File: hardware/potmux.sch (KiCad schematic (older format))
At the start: 8 parts, among them P1 SOCKET_LEFT, P3 SOCKET_RIGHT, P4 KEYMAN64, U1 4052, U2 4052

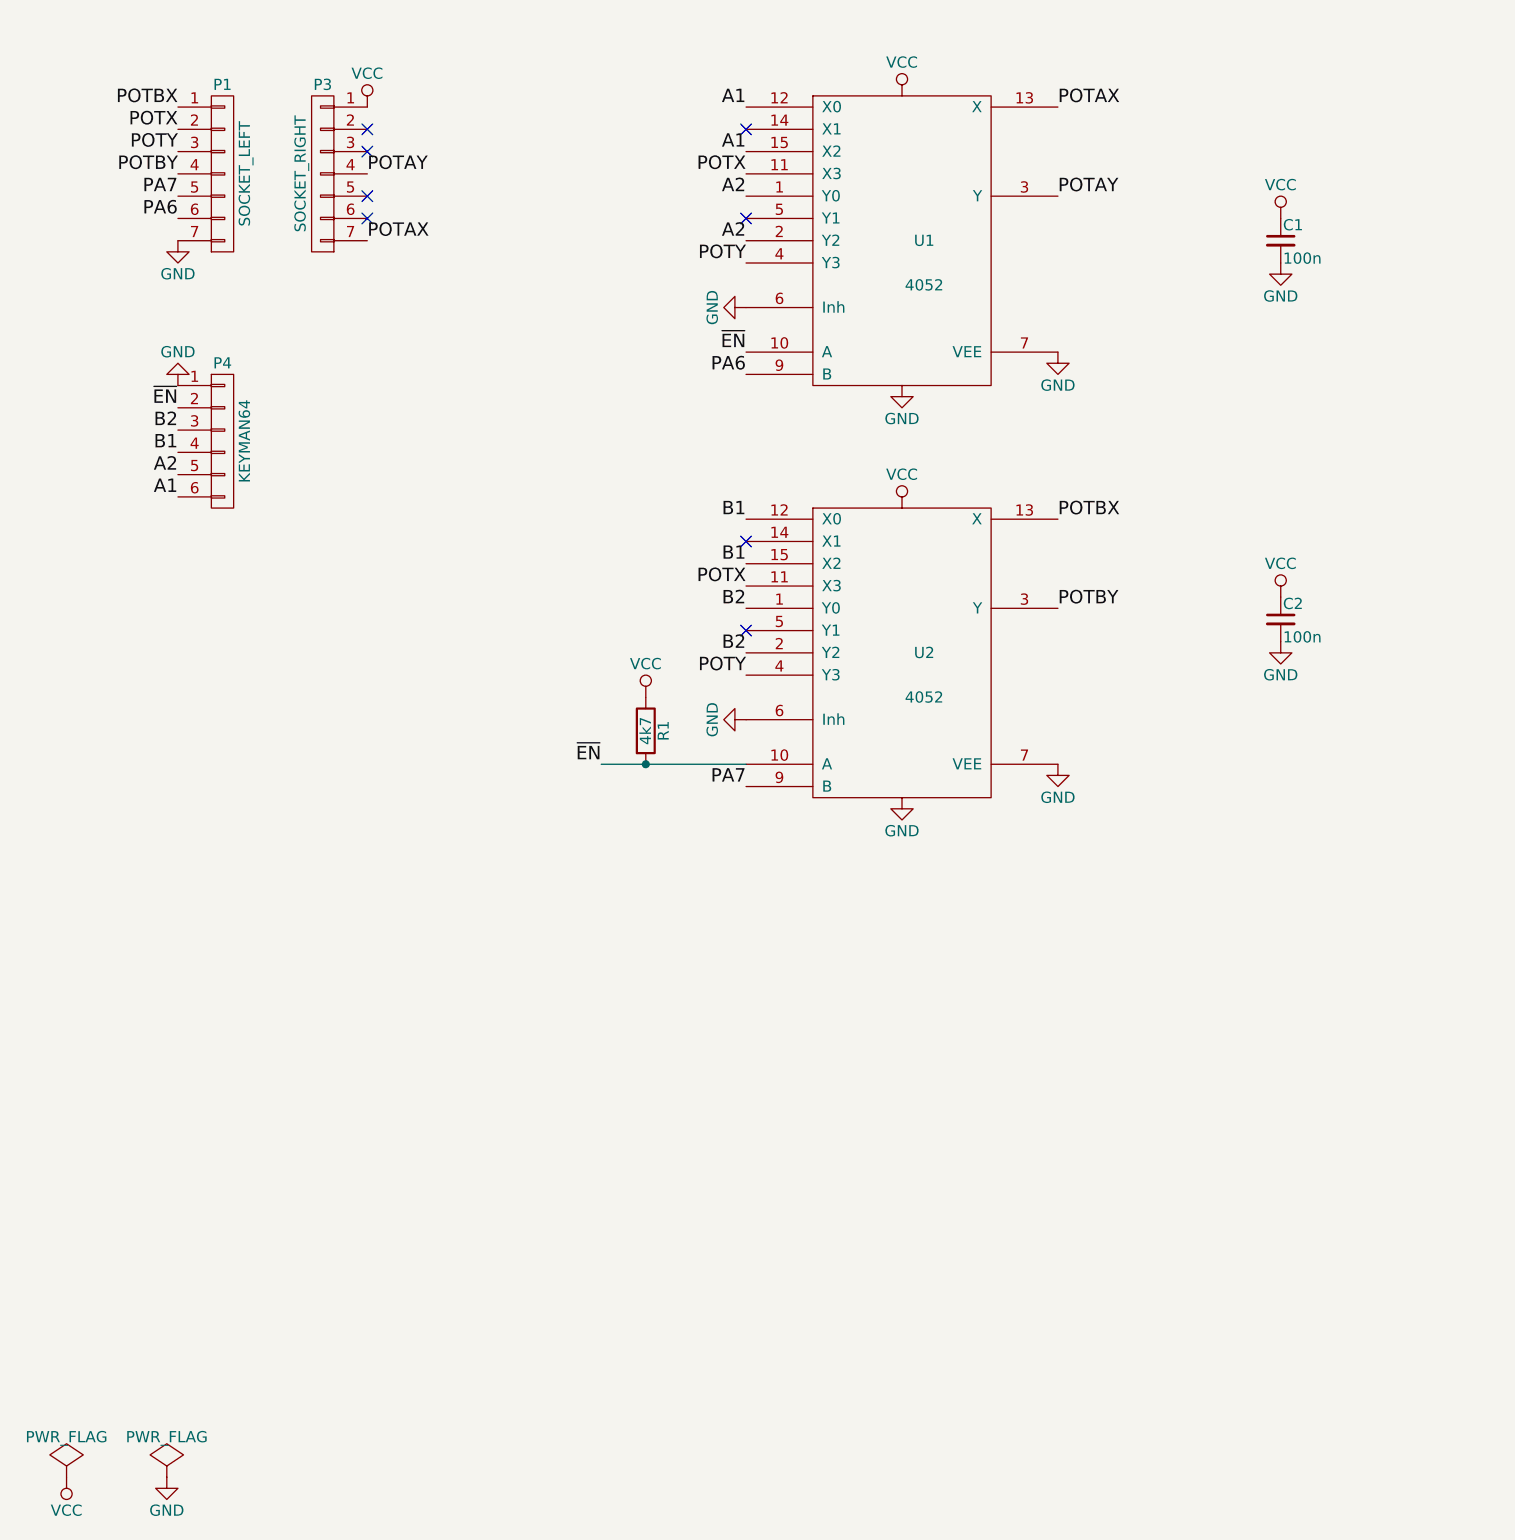
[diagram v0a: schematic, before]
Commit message: Improved layout, silk screen
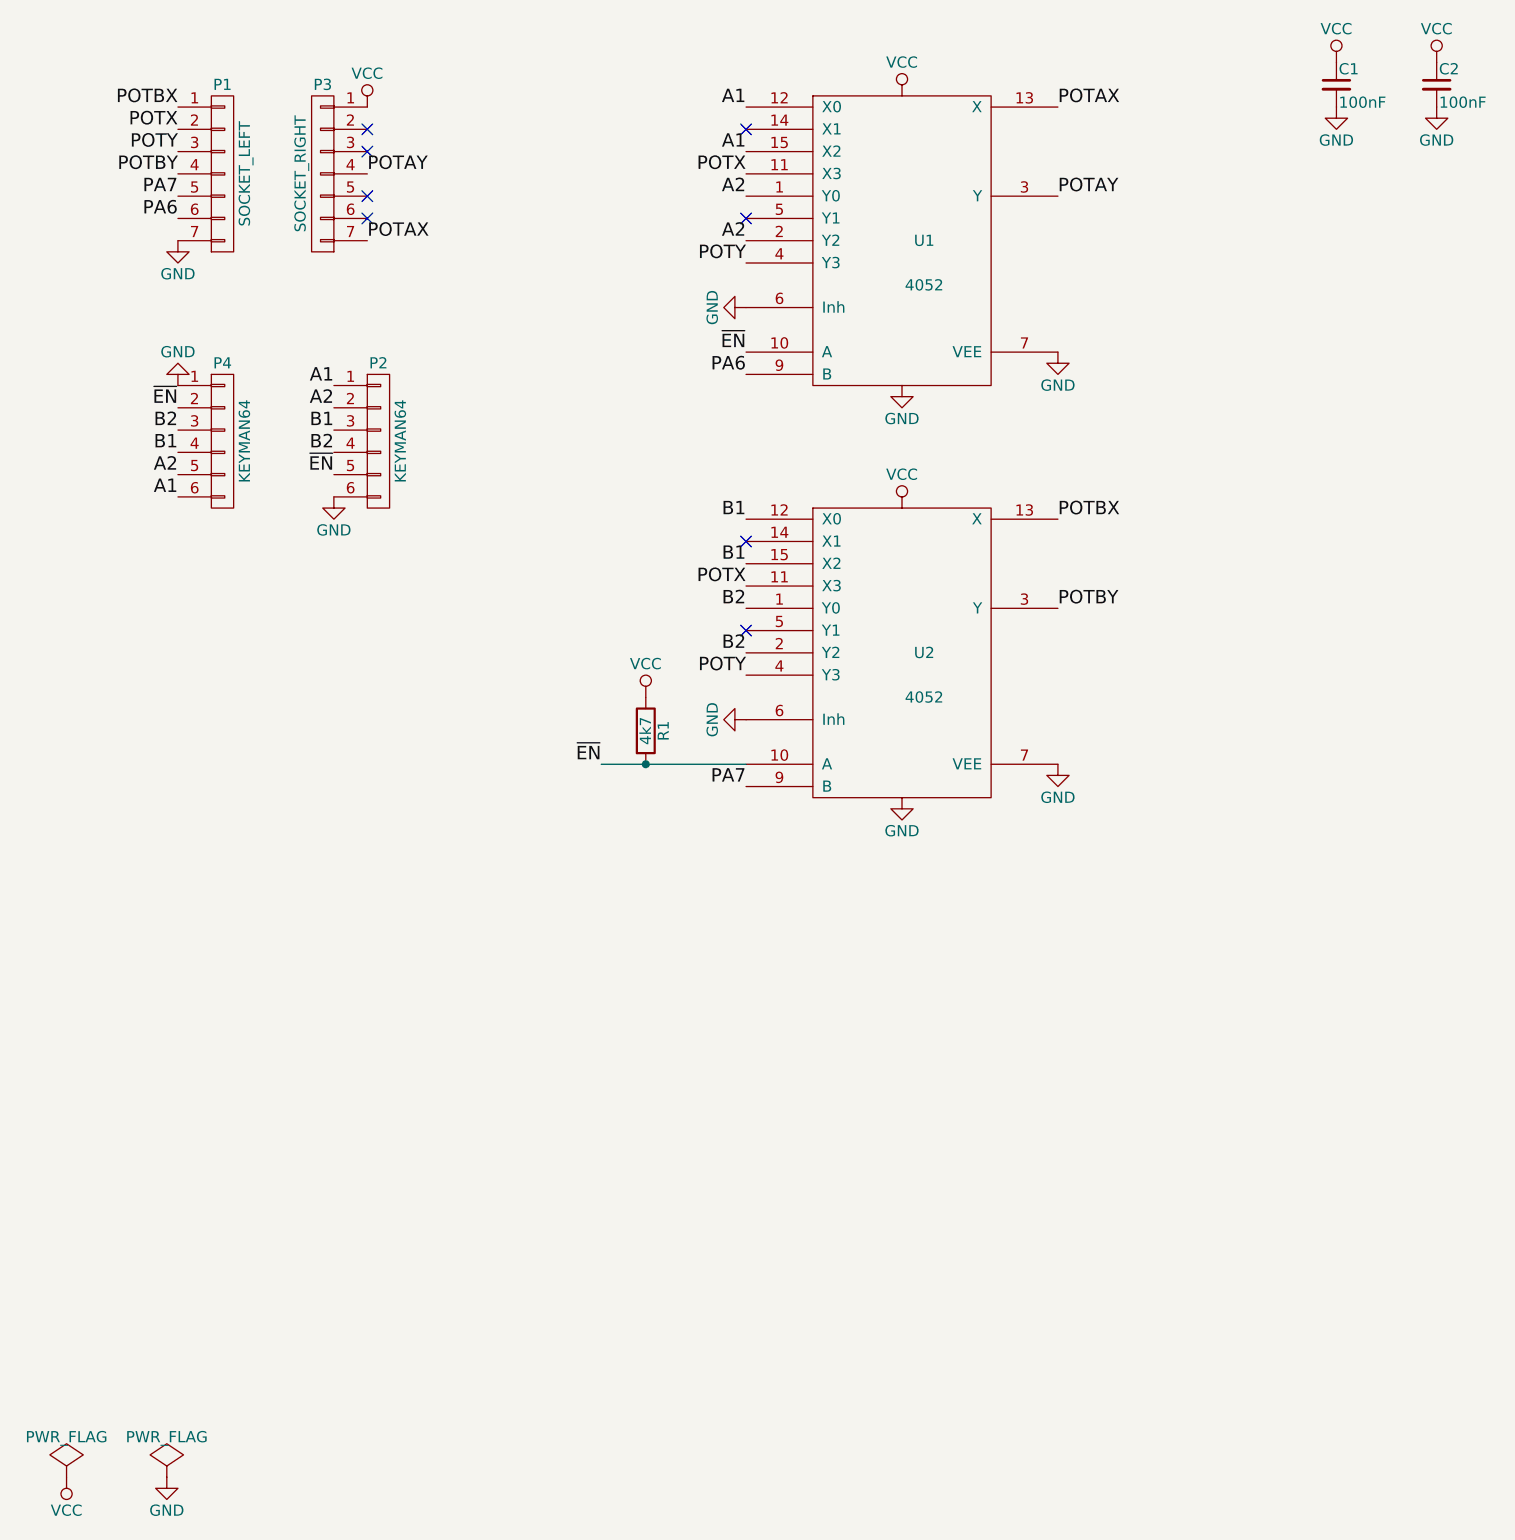
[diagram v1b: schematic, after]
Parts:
- added P2: KEYMAN64, Pin_Headers:Pin_Header_Angled_1x06_Pitch2.54mm, symbol CONN_01X06
- C1, C2: value 100n -> 100nF; footprint Capacitors_ThroughHole:C_Disc_D3.0mm_W1.6mm_P2.50mm -> Capacitors_SMD:C_0805_HandSoldering
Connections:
- net A1: now also P2.1 (P1)
- net A2: now also P2.2 (P2)
- net B1: now also P2.3 (P3)
- net B2: now also P2.4 (P4)
- net GND: now also P2.6 (P6)
- net ~EN: now also P2.5 (P5)
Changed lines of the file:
@@
 $Comp
 L VCC #PWR011
-U 1 1 580E8B82
-P 6200 1850
-F 0 "#PWR011" H 6200 1700 50  0001 C CNN
-F 1 "VCC" H 6200 2000 50  0000 C CNN
-F 2 "" H 6200 1850 50  0000 C CNN
-F 3 "" H 6200 1850 50  0000 C CNN
-	1    6200 1850
-	1    0    0    -1
-$EndComp
-$Comp
-L C_Small C1
-U 1 1 580E8BA8
-P 6200 1950
-F 0 "C1" H 6210 2020 50  0000 L CNN
-F 1 "100n" H 6210 1870 50  0000 L CNN
-F 2 "Capacitors_ThroughHole:C_Disc_D3.0mm_W1.6mm_P2.50mm" H 6200 1950 50  0001 C CNN
-F 3 "" H 6200 1950 50  0000 C CNN
-	1    6200 1950
-	1    0    0    -1
-$EndComp
-$Comp
-L GND #PWR012
-U 1 1 580E8C87
-P 6200 2050
-F 0 "#PWR012" H 6200 1800 50  0001 C CNN
-F 1 "GND" H 6200 1900 50  0000 C CNN
-F 2 "" H 6200 2050 50  0000 C CNN
-F 3 "" H 6200 2050 50  0000 C CNN
-	1    6200 2050
-	1    0    0    -1
-$EndComp
-$Comp
-L VCC #PWR013
 U 1 1 580E7B51
 P 2100 1350
-F 0 "#PWR013" H 2100 1200 50  0001 C CNN
+F 0 "#PWR011" H 2100 1200 50  0001 C CNN
 F 1 "VCC" H 2100 1500 50  0000 C CNN
 F 2 "" H 2100 1350 50  0000 C CNN
@@
 $EndComp
 $Comp
-L VCC #PWR014
+L VCC #PWR012
 U 1 1 580E9B1D
 P 4500 1300
-F 0 "#PWR014" H 4500 1150 50  0001 C CNN
+F 0 "#PWR012" H 4500 1150 50  0001 C CNN
 F 1 "VCC" H 4500 1450 50  0000 C CNN
 F 2 "" H 4500 1300 50  0000 C CNN
@@
 $EndComp
 $Comp
-L GND #PWR015
+L GND #PWR013
 U 1 1 580E9B87
 P 4500 2600
-F 0 "#PWR015" H 4500 2350 50  0001 C CNN
+F 0 "#PWR013" H 4500 2350 50  0001 C CNN
 F 1 "GND" H 4500 2450 50  0000 C CNN
 F 2 "" H 4500 2600 50  0000 C CNN
@@
 $EndComp
 $Comp
-L VCC #PWR016
+L VCC #PWR014
 U 1 1 580E9C6A
 P 4500 3150
-F 0 "#PWR016" H 4500 3000 50  0001 C CNN
+F 0 "#PWR014" H 4500 3000 50  0001 C CNN
 F 1 "VCC" H 4500 3300 50  0000 C CNN
 F 2 "" H 4500 3150 50  0000 C CNN
@@
 $EndComp
 $Comp
-L GND #PWR017
+L GND #PWR015
 U 1 1 580E9C8D
 P 4500 4450
-F 0 "#PWR017" H 4500 4200 50  0001 C CNN
+F 0 "#PWR015" H 4500 4200 50  0001 C CNN
 F 1 "GND" H 4500 4300 50  0000 C CNN
 F 2 "" H 4500 4450 50  0000 C CNN
@@
 NoConn ~ 2100 1850
 $Comp
-L GND #PWR018
+L GND #PWR016
 U 1 1 5901CAA6
 P 1250 2600
-F 0 "#PWR018" H 1250 2350 50  0001 C CNN
+F 0 "#PWR016" H 1250 2350 50  0001 C CNN
 F 1 "GND" H 1250 2450 50  0000 C CNN
 F 2 "" H 1250 2600 50  0000 C CNN
@@
 $EndComp
 $Comp
+L GND #PWR017
+U 1 1 5979EB0A
+P 1950 3100
+F 0 "#PWR017" H 1950 2850 50  0001 C CNN
+F 1 "GND" H 1950 2950 50  0000 C CNN
+F 2 "" H 1950 3100 50  0000 C CNN
+F 3 "" H 1950 3100 50  0000 C CNN
+	1    1950 3100
+	-1   0    0    -1
+$EndComp
+Text Label 1950 3000 2    60   ~ 0
+~EN
+Text Label 1950 2900 2    60   ~ 0
+B2
+Text Label 1950 2800 2    60   ~ 0
+B1
+Text Label 1950 2700 2    60   ~ 0
+A2
+Text Label 1950 2600 2    60   ~ 0
+A1
+$Comp
+L CONN_01X06 P2
+U 1 1 5979EB15
+P 2150 2850
+F 0 "P2" H 2150 3200 50  0000 C CNN
+F 1 "KEYMAN64" V 2250 2850 50  0000 C CNN
+F 2 "Pin_Headers:Pin_Header_Angled_1x06_Pitch2.54mm" H 2150 2850 50  0001 C CNN
+F 3 "" H 2150 2850 50  0000 C CNN
+	1    2150 2850
+	1    0    0    -1
+$EndComp
+$Comp
+L C_Small C1
+U 1 1 5979F45F
+P 6450 1250
+F 0 "C1" H 6460 1320 50  0000 L CNN
+F 1 "100nF" H 6460 1170 50  0000 L CNN
+F 2 "Capacitors_SMD:C_0805_HandSoldering" H 6450 1250 50  0001 C CNN
+F 3 "" H 6450 1250 50  0000 C CNN
+	1    6450 1250
+	1    0    0    -1
+$EndComp
+$Comp
+L VCC #PWR018
+U 1 1 5979F527
+P 6450 1150
+F 0 "#PWR018" H 6450 1000 50  0001 C CNN
+F 1 "VCC" H 6450 1300 50  0000 C CNN
+F 2 "" H 6450 1150 50  0000 C CNN
+F 3 "" H 6450 1150 50  0000 C CNN
+	1    6450 1150
+	1    0    0    -1
+$EndComp
+$Comp
 L GND #PWR019
-U 1 1 580E8E34
-P 6200 3750
-F 0 "#PWR019" H 6200 3500 50  0001 C CNN
-F 1 "GND" H 6200 3600 50  0000 C CNN
-F 2 "" H 6200 3750 50  0000 C CNN
-F 3 "" H 6200 3750 50  0000 C CNN
-	1    6200 3750
+U 1 1 5979F573
+P 6450 1350
+F 0 "#PWR019" H 6450 1100 50  0001 C CNN
+F 1 "GND" H 6450 1200 50  0000 C CNN
+F 2 "" H 6450 1350 50  0000 C CNN
+F 3 "" H 6450 1350 50  0000 C CNN
+	1    6450 1350
 	1    0    0    -1
 $EndComp
 $Comp
 L C_Small C2
-U 1 1 580E8E2E
-P 6200 3650
-F 0 "C2" H 6210 3720 50  0000 L CNN
-F 1 "100n" H 6210 3570 50  0000 L CNN
-F 2 "Capacitors_ThroughHole:C_Disc_D3.0mm_W1.6mm_P2.50mm" H 6200 3650 50  0001 C CNN
-F 3 "" H 6200 3650 50  0000 C CNN
-	1    6200 3650
+U 1 1 5979F66F
+P 6900 1250
+F 0 "C2" H 6910 1320 50  0000 L CNN
+F 1 "100nF" H 6910 1170 50  0000 L CNN
+F 2 "Capacitors_SMD:C_0805_HandSoldering" H 6900 1250 50  0001 C CNN
+F 3 "" H 6900 1250 50  0000 C CNN
+	1    6900 1250
 	1    0    0    -1
 $EndComp
 $Comp
 L VCC #PWR020
-U 1 1 580E8E28
-P 6200 3550
-F 0 "#PWR020" H 6200 3400 50  0001 C CNN
-F 1 "VCC" H 6200 3700 50  0000 C CNN
-F 2 "" H 6200 3550 50  0000 C CNN
-F 3 "" H 6200 3550 50  0000 C CNN
-	1    6200 3550
+U 1 1 5979F675
+P 6900 1150
+F 0 "#PWR020" H 6900 1000 50  0001 C CNN
+F 1 "VCC" H 6900 1300 50  0000 C CNN
+F 2 "" H 6900 1150 50  0000 C CNN
+F 3 "" H 6900 1150 50  0000 C CNN
+	1    6900 1150
 	1    0    0    -1
 $EndComp
+$Comp
+L GND #PWR021
+U 1 1 5979F67B
+P 6900 1350
+F 0 "#PWR021" H 6900 1100 50  0001 C CNN
+F 1 "GND" H 6900 1200 50  0000 C CNN
+F 2 "" H 6900 1350 50  0000 C CNN
+F 3 "" H 6900 1350 50  0000 C CNN
+	1    6900 1350
+	1    0    0    -1
+$EndComp
